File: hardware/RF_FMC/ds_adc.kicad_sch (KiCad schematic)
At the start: 75 parts, among them J1 Conn_Coaxial, Q1 SI1539CDL-T1-GE3, T1 PWB2010L, T2 Macom_ETC1-1-13, U5 REF5025IDGK, U6 LTC2216

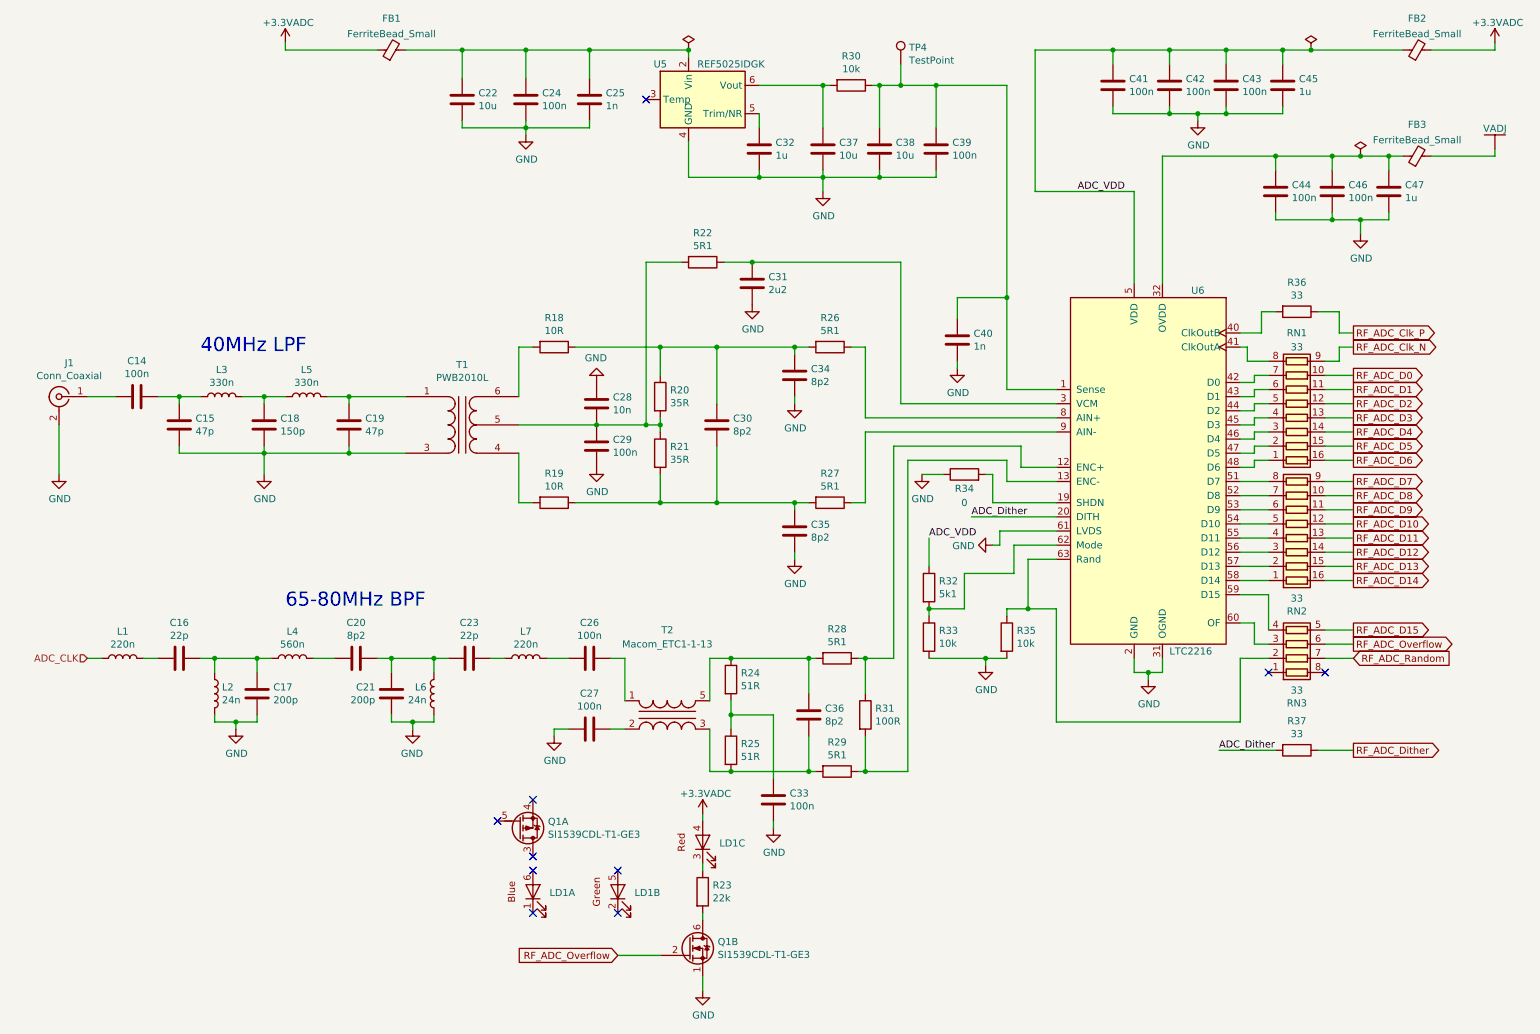
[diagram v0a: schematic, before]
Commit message: Started on ADC layout
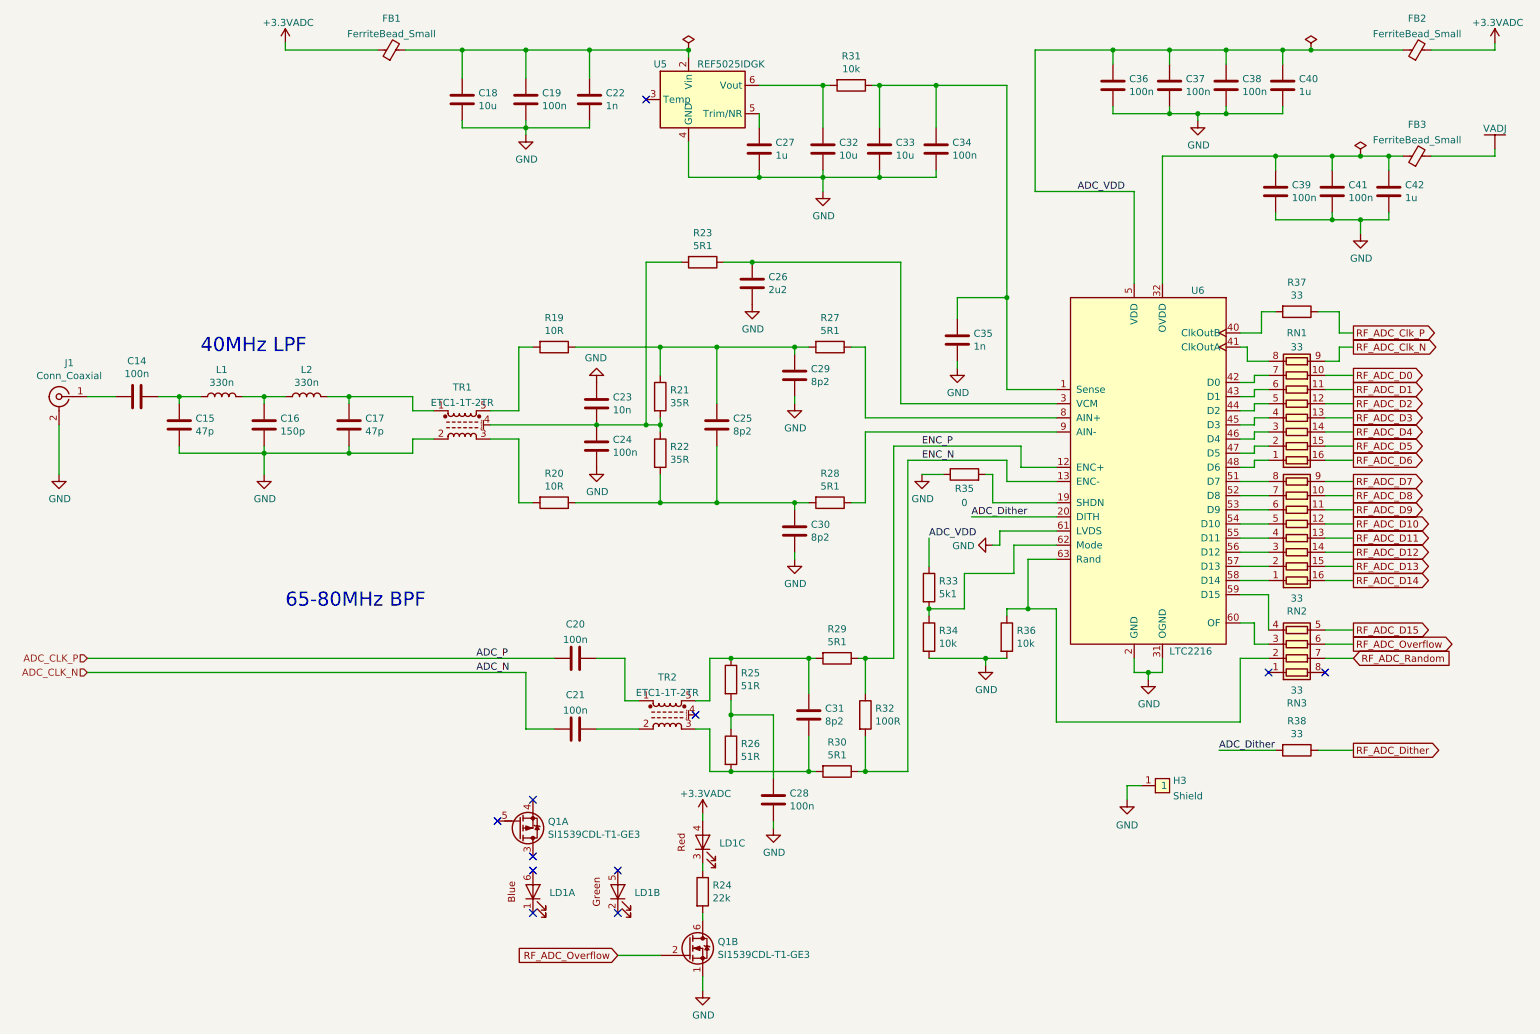
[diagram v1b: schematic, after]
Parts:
- removed C16, C23: 22p, Capacitor_SMD:C_0402_1005Metric, symbol Device:C
- removed C17: 200p, Capacitor_SMD:C_0402_1005Metric, symbol Device:C
- removed C26, C27: 100n, Capacitor_SMD:C_0402_1005Metric, symbol Device:C
- removed L1, L7: 220n, Inductor_SMD:L_0603_1608Metric, symbol Device:L
- removed L2, L6: 24n, Inductor_SMD:L_0603_1608Metric, symbol Device:L
- removed L4: 560n, Inductor_SMD:L_0603_1608Metric, symbol Device:L
- removed T1: PWB2010L, Transformer_WUT:Coilcraft_PWB, symbol Transformer_WUT:Coilcraft_PWB_Type-B
- removed T2: Macom_ETC1-1-13, Transformer_SMD:Transformer_MACOM_SM-22, symbol Transformer_WUT:Macom_ETC1-1-13
- removed TP4: TestPoint, TestPoint:TestPoint_Pad_D1.5mm, symbol Connector:TestPoint
- added H3: Shield, Shield_WUT:Shield_Masach_MS477-10_47.7x18.2x4mm_TH.step, symbol Shield_WUT:Shield
- added TR1, TR2: ETC1-1T-2TR, Transformer_WUT:Macom_ETC-1xx, symbol Transformer:ETC1-1-13
- C20: value 8p2 -> 100n
- C21: value 200p -> 100n
- R25: renamed from R24; footprint Resistor_SMD:R_0201_0603Metric -> Resistor_SMD:R_0402_1005Metric
- R26: renamed from R25; footprint Resistor_SMD:R_0201_0603Metric -> Resistor_SMD:R_0402_1005Metric
- R32: renamed from R31; footprint Resistor_SMD:R_0402_1005Metric -> Resistor_SMD:R_0201_0603Metric
- renumbered C18 to C16, C19 to C17, C22 to C18, C24 to C19, C25 to C22, C28 to C23, C29 to C24, C30 to C25, C31 to C26, C32 to C27, C33 to C28, C34 to C29, C35 to C30, C36 to C31, C37 to C32, C38 to C33, C39 to C34, C40 to C35, C41 to C36, C42 to C37, C43 to C38, C44 to C39, C45 to C40, C46 to C41, C47 to C42, L3 to L1, L5 to L2, R18 to R19, R19 to R20, R20 to R21, R21 to R22, R22 to R23, R23 to R24, R26 to R27, R27 to R28, R28 to R29, R29 to R30, R30 to R31, R32 to R33, R33 to R34, R34 to R35, R35 to R36, R36 to R37, R37 to R38
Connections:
- net GND: now also H3.1, TR1.2; no longer C21.2
- net at C31.2, R26.2, R30.2: now also TR2.3
- net at C31.1, R25.1, R29.2: now also TR2.5
- net ENC_N: now reaches R30.1, R32.2, U6.13 (ENC-)
- net at C23.2, C24.1, R21.2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: now also TR1.4 (MP)
- net at C17.1, L2.2: now also TR1.1
- net ADC_CLK_N: now reaches C21.1
- net ADC_CLK_N: no longer C20.1
- net at R20.2: now also TR1.3
- net at C20.2: now also TR2.1
- net ENC_P: now reaches R29.1, R32.1, U6.12 (ENC+)
- net at R19.2: now also TR1.5
- new net: C21.2, TR2.2
- new net ADC_CLK_P: C20.1
- no-connect marks 10 -> 11
